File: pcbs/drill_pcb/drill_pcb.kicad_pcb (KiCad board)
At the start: 2 copper layers, 85 parts, among them J301 Screw_Terminal_01x06, J302 motor1, J303 Screw_Terminal_01x03, J304 Screw_Terminal_01x03, J305 Screw_Terminal_01x06, J306 motor2, J307 TOF_senzor, J308 Screw_Terminal_01x03, J309 Screw_Terminal_01x03, J401 Screw_Terminal_01x04, J402 Screw_Terminal_01x06, J403 Screw_Terminal_01x04, SW101 RPi reset, SW401 SW_Push, SW402 SW_Push, SW403 SW_Push, U101 PCA9306, U102 Pico, U201 IFX007T, U202 IFX007T, U203 ACS712xLCTR-20A, U401 HT75xx-1-SOT89

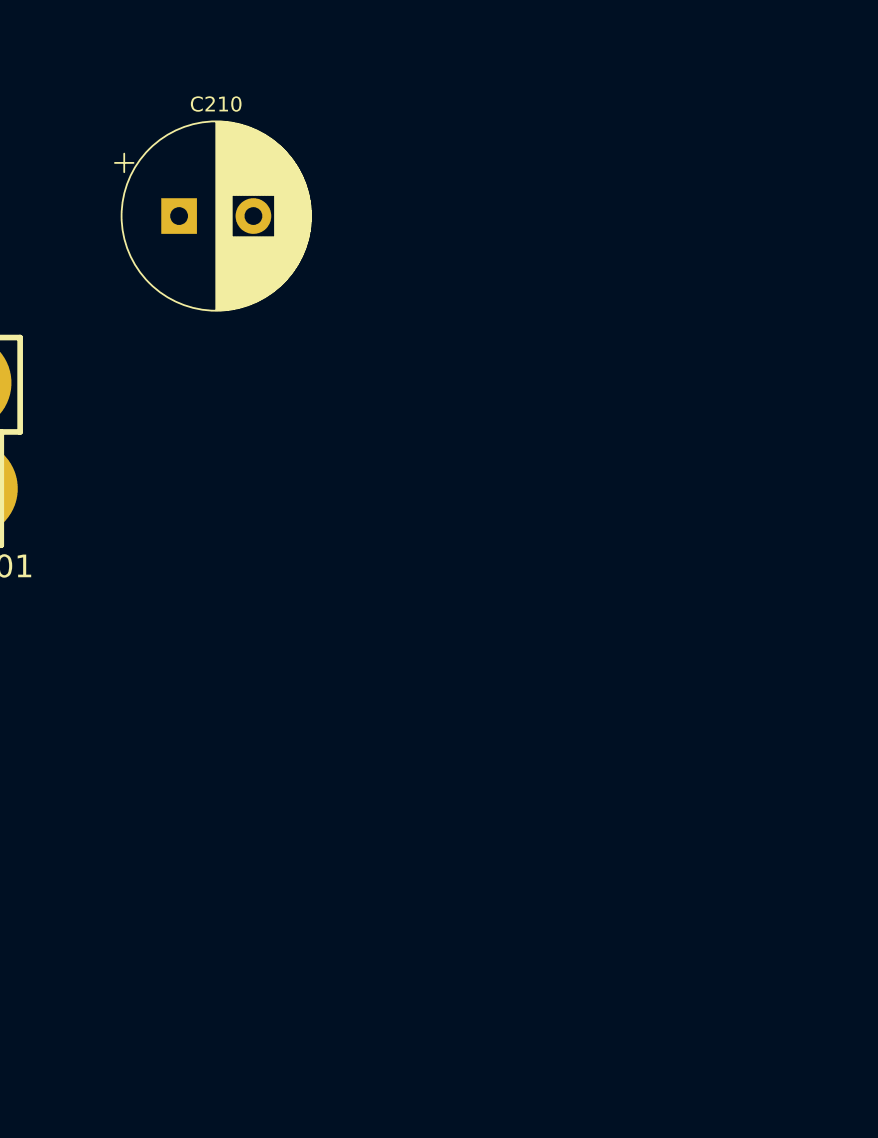
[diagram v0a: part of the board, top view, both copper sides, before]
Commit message: added motor heatsink footprint
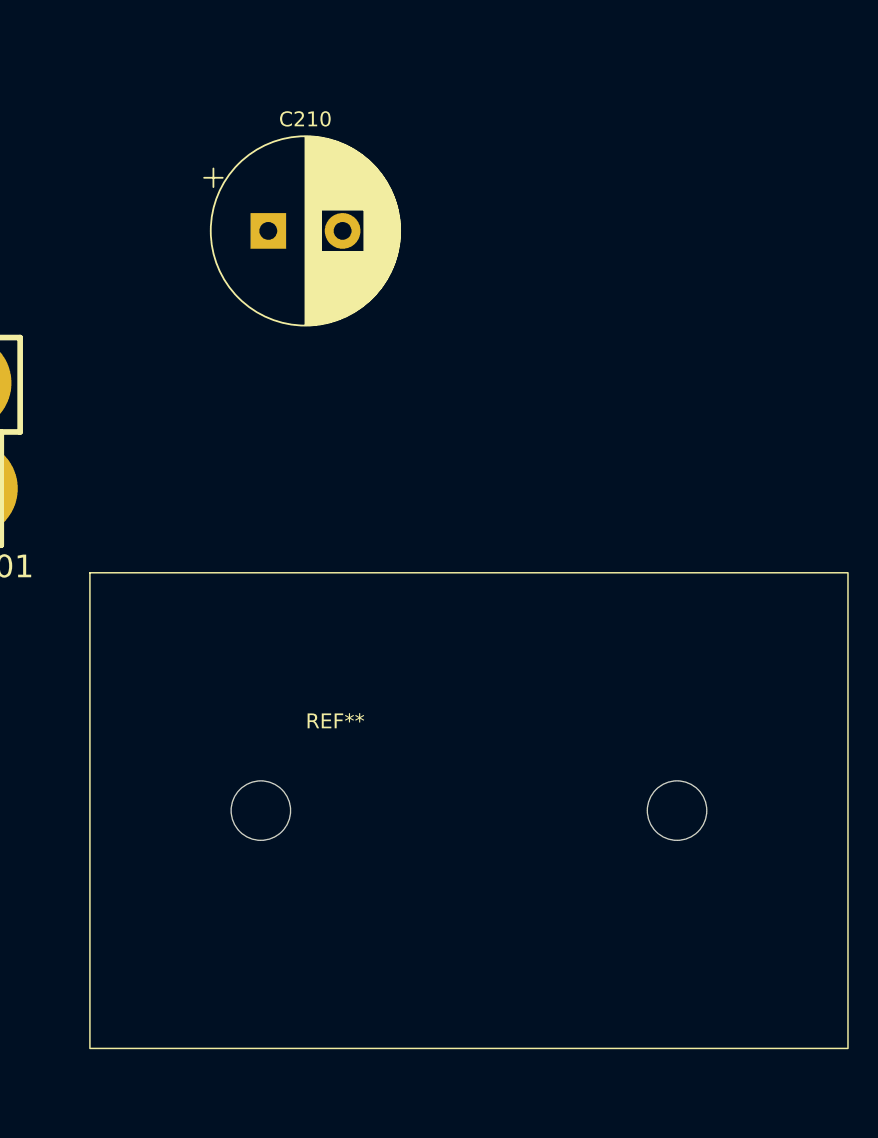
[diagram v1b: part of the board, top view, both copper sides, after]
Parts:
- added REF**: drill_heatsink, heatsink:drill_heatsink, F.Cu at (348.0, 85.0)
- moved C210 6.08 mm to (360.0, 62.0)
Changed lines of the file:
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@@
 		)
 	)
+	(footprint "heatsink:drill_heatsink"
+		(layer "F.Cu")
+		(at 348 85)
+		(property "Reference" "REF**"
+			(at 16.5 10 0)
+			(unlocked yes)
+			(layer "F.SilkS")
+			(effects
+				(font
+					(size 1 1)
+					(thickness 0.1)
+				)
+			)
+		)
+		(property "Value" "drill_heatsink"
+			(at 16.5 11.5 0)
+			(unlocked yes)
+			(layer "F.Fab")
+			(effects
+				(font
+					(size 1 1)
+					(thickness 0.15)
+				)
+			)
+		)
+		(property "Footprint" "heatsink:drill_heatsink"
+			(at 16.5 10.5 0)
+			(unlocked yes)
+			(layer "F.Fab")
+			(hide yes)
+			(effects
+				(font
+					(size 1 1)
+					(thickness 0.15)
+				)
+			)
+		)
+		(property "Datasheet" ""
+			(at 16.5 10.5 0)
+			(unlocked yes)
+			(layer "F.Fab")
+			(hide yes)
+			(effects
+				(font
+					(size 1 1)
+					(thickness 0.15)
+				)
+			)
+		)
+		(property "Description" ""
+			(at 16.5 10.5 0)
+			(unlocked yes)
+			(layer "F.Fab")
+			(hide yes)
+			(effects
+				(font
+					(size 1 1)
+					(thickness 0.15)
+				)
+			)
+		)
+		(attr smd)
+		(fp_rect
+			(start 0 0)
+			(end 51 32)
+			(stroke
+				(width 0.1)
+				(type default)
+			)
+			(fill none)
+			(layer "F.SilkS")
+		)
+		(fp_text user "${REFERENCE}"
+			(at 16.5 13 0)
+			(unlocked yes)
+			(layer "F.Fab")
+			(effects
+				(font
+					(size 1 1)
+					(thickness 0.15)
+				)
+			)
+		)
+		(pad "" np_thru_hole circle
+			(at 11.5 16)
+			(size 4 4)
+			(drill 4)
+			(layers "F&B.Cu" "*.Mask")
+		)
+		(pad "" np_thru_hole circle
+			(at 39.5 16)
+			(size 4 4)
+			(drill 4)
+			(layers "F&B.Cu" "*.Mask")
+		)
+	)
 	(footprint "Capacitor_THT:CP_Radial_D5.0mm_P2.50mm"
 		(layer "F.Cu")
@@
 		(tags "Diode SMC (DO-214AB) Handsoldering")
 		(property "Reference" "D101"
-			(at 0 -4.1 360)
+			(at 0 -4.1 0)
 			(layer "F.SilkS")
 			(effects
@@
 		)
 		(property "Value" "3A"
-			(at 0 4.2 360)
+			(at 0 4.2 0)
 			(layer "F.Fab")
 			(effects
@@
 		)
 		(fp_text user "${REFERENCE}"
-			(at 0 -1.5 360)
+			(at 0 -1.5 0)
 			(layer "F.Fab")
 			(effects
@@
 	(footprint "Capacitor_THT:CP_Radial_D12.5mm_P5.00mm"
 		(layer "F.Cu")
-		(at 354 61)
+		(at 360 62)
 		(descr "CP, Radial series, Radial, pin pitch=5.00mm, , diameter=12.5mm, Electrolytic Capacitor")
 		(tags "CP Radial series Radial pin pitch 5.00mm  diameter 12.5mm Electrolytic Capacitor")
@@
 		(tags "car blade fuse")
 		(property "Reference" "F101"
-			(at 4.65 -3.9 360)
+			(at 4.65 -3.9 0)
 			(layer "F.SilkS")
 			(effects
@@
 		)
 		(property "Value" "5A"
-			(at 4.6 4 360)
+			(at 4.6 4 0)
 			(layer "F.Fab")
 			(effects
@@
 		)
 		(fp_text user "${REFERENCE}"
-			(at 4.75 -1.5 360)
+			(at 4.75 -1.5 0)
 			(layer "F.Fab")
 			(effects

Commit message: Mostly finished PCB v1.0.0 Missing strain gauge control circuit
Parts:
- removed C403, C404, C405: 10n, Capacitor_THT:C_Disc_D4.7mm_W2.5mm_P5.00mm
- removed D101: 3A, Diode_SMD:D_SMC_Handsoldering
- removed D401: 1N4007, Diode_THT:D_DO-41_SOD81_P10.16mm_Horizontal
- removed D402, D403, D404: SFH4550, LED_THT:LED_D5.0mm_IRGrey
- removed J303, J304, J308, J309: Screw_Terminal_01x03, Connector_JST:JST_XH_S3B-XH-A-1_1x03_P2.50mm_Horizontal
- removed J305: Screw_Terminal_01x06, Connector_JST:JST_XH_S6B-XH-A-1_1x06_P2.50mm_Horizontal
- removed JST201: Thermometer, Connector_JST:JST_XH_B3B-XH-A_1x03_P2.50mm_Vertical
- removed R401, R402, R403, R404: 10k, Resistor_THT:R_Axial_DIN0207_L6.3mm_D2.5mm_P10.16mm_Horizontal
- removed SW401, SW402, SW403: SW_Push, Button_Switch_THT:SW_PUSH_6mm
- removed U101: PCA9306, drill_i2c_level_shifter:i2c_levl_shifter
- added D203: SMAJ24A, Diode_SMD:D_SMA, F.Cu at (99.0, 154.0)
- added J201: Thermometer, Connector_JST:JST_XH_B3B-XH-A_1x03_P2.50mm_Vertical, F.Cu at (87.5, 193.0)
- added REF**: MountingHole_3.2mm_M3, MountingHole:MountingHole_3.2mm_M3, F.Cu at (285.0, 105.0)
- added REF**: MountingHole_3.2mm_M3, MountingHole:MountingHole_3.2mm_M3, F.Cu at (55.0, 105.0)
- added REF**: MountingHole_3.2mm_M3, MountingHole:MountingHole_3.2mm_M3, F.Cu at (55.0, 195.0)
- added REF**: MountingHole_3.2mm_M3, MountingHole:MountingHole_3.2mm_M3, F.Cu at (285.0, 195.0)
- added U1: FXMA108, drill_i2c_level_shifter:logic_convertor_8ch, F.Cu at (147.0, 111.0)
- C202, C203, C207, R202, R203, R206, R207, R210, R301, REF**: moved to B.Cu
- J401, J403: footprint TerminalBlock_TE-Connectivity:TerminalBlock_TE_282834-4_1x04_P2.54mm_Horizontal -> Connector_JST:JST_XH_B4B-XH-A_1x04_P2.50mm_Vertical
- J402: footprint TerminalBlock_TE-Connectivity:TerminalBlock_TE_282834-6_1x06_P2.54mm_Horizontal -> Connector_JST:JST_XH_B6B-XH-A_1x06_P2.50mm_Vertical
- moved D201 305.8 mm to (56.0, 133.5), turned to 180 degrees
- moved D202 300.0 mm to (54.5, 113.3), turned to 180 degrees
- moved U203 296.2 mm to (82.1, 180.0)
- moved Dean201 289.1 mm to (74.5, 192.6), turned to -90 degrees
- moved C210 286.6 mm to (86.0, 146.0), turned to 90 degrees
- moved U202 286.0 mm to (71.3, 165.7), turned to -90 degrees
- moved C202 282.8 mm to (61.9, 143.5)
- moved C206 282.2 mm to (55.0, 127.0)
- moved U201 281.2 mm to (82.1, 165.7), turned to -90 degrees
- moved C208 280.9 mm to (53.5, 116.8)
- moved C203 276.9 mm to (67.1, 143.5), turned to 180 degrees
- moved C205 276.3 mm to (69.1, 154.5), turned to 180 degrees
- moved R202 276.2 mm to (62.0, 140.5), turned to 180 degrees
- moved C201 276.1 mm to (87.0, 183.5), turned to 90 degrees
- moved R208 275.8 mm to (55.0, 130.0), turned to 180 degrees
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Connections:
- A201 pad 28: unconnected-(A201-~{RESET}-Pad28) -> /Motor control/RESET
- A201 pad 3: unconnected-(A201-~{RESET}-Pad3) -> /Motor control/RESET
- A301 pad 28: unconnected-(A301-~{RESET}-Pad28) -> /Linear drive control/RESET
- A301 pad 3: unconnected-(A301-~{RESET}-Pad3) -> /Linear drive control/RESET
- A401 pad 12: BTN_RED -> unconnected-(A401-D9-Pad12)
- A401 pad 13: BTN_YEL -> unconnected-(A401-D10-Pad13)
- A401 pad 28: unconnected-(A401-~{RESET}-Pad28) -> /Storage and weighing/RESET
- A401 pad 3: unconnected-(A401-~{RESET}-Pad3) -> /Storage and weighing/RESET
- A401 pad 7: BTN_GRN -> unconnected-(A401-D4-Pad7)
- A402 pad 8: +23,3V -> +24V
- C401 pad 1: +23,3V -> +24V
- F102 pad 2: Net-(D101-A) -> Net-(V101-+Vin)
- U102 pad 10: unconnected-(U102-GPIO7-Pad10) -> Net-(U1-A3)
- U102 pad 11: unconnected-(U102-GPIO8-Pad11)_1 -> Net-(U1-A2)
- U102 pad 12: unconnected-(U102-GPIO9-Pad12)_1 -> Net-(U1-A1)
- U401 pad 2: +23,3V -> +24V
- V101 pad 1: Net-(D101-K) -> Net-(V101-+Vin)
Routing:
- net GND: track 0.00 -> 938.0 mm, vias 0 -> 7
- net +5V: track 0.00 -> 548.3 mm, vias 0 -> 1
- net +24V: track 0.00 -> 287.3 mm
- net /Linear drive control/SDA: track 0.00 -> 196.2 mm, vias 0 -> 2
- net /Linear drive control/SCL: track 0.00 -> 194.0 mm
- net Net-(A201-A3): track 0.00 -> 141.6 mm, vias 0 -> 1
- net Net-(A301-A1): track 0.00 -> 136.6 mm
- net Net-(A301-D11): track 0.00 -> 126.3 mm
- net Net-(A201-A0): track 0.00 -> 115.4 mm, vias 0 -> 2
- net Net-(A301-A0): track 0.00 -> 114.6 mm
- net /Storage and weighing/RESET: track 0.00 -> 113.7 mm
- net Net-(A301-D9): track 0.00 -> 113.7 mm
- net Net-(A201-D7): track 0.00 -> 100.3 mm, vias 0 -> 1
- net Net-(A301-D10): track 0.00 -> 96.9 mm
- net Net-(A301-D5): track 0.00 -> 96.3 mm
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- added copper zone on B.Cu, net Net-(Dean201-Pin_2)
- added copper zone on B.Cu, net Net-(U201-OUT-Pad8)
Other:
- board outline added: 240 x 100 mm
- board text added: "Brno Drilling Space Mission v1.0.0"
- board text added: "ŠLÍMA SMRDÍ"

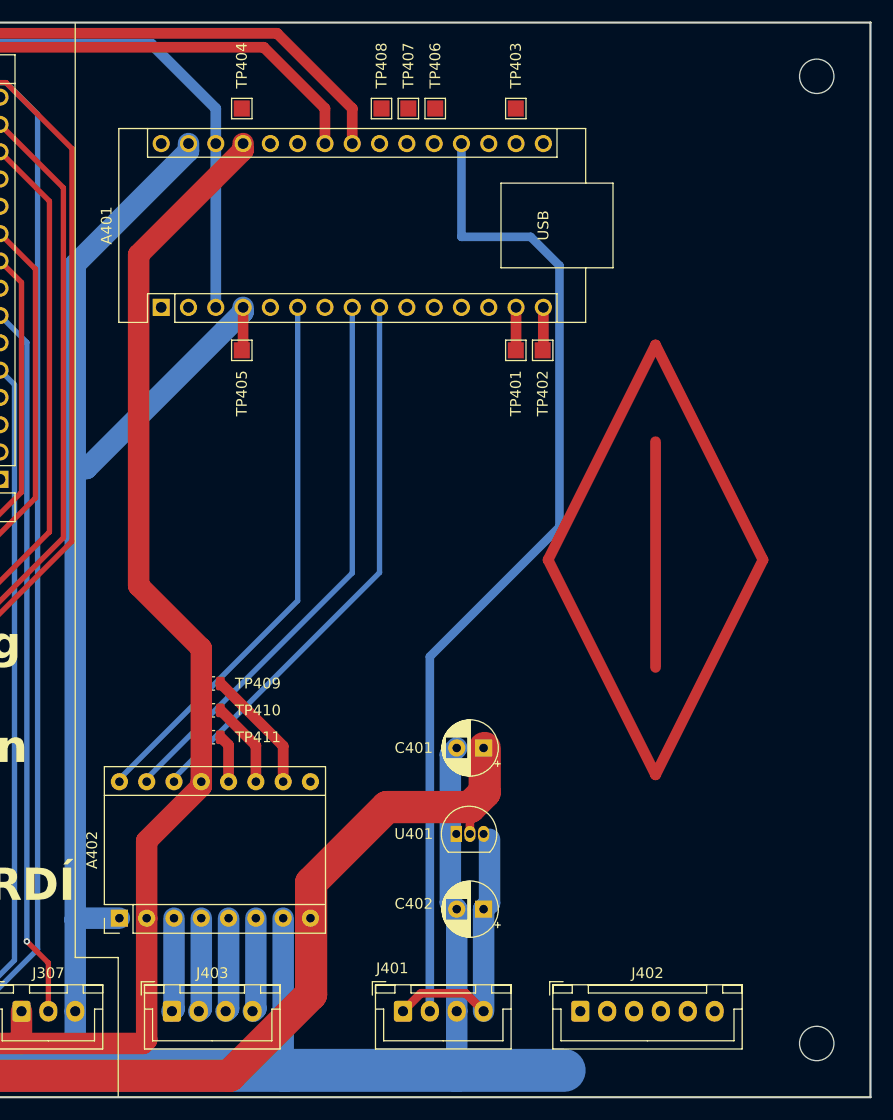
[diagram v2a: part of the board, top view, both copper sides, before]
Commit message: update pouzdra konvertoru
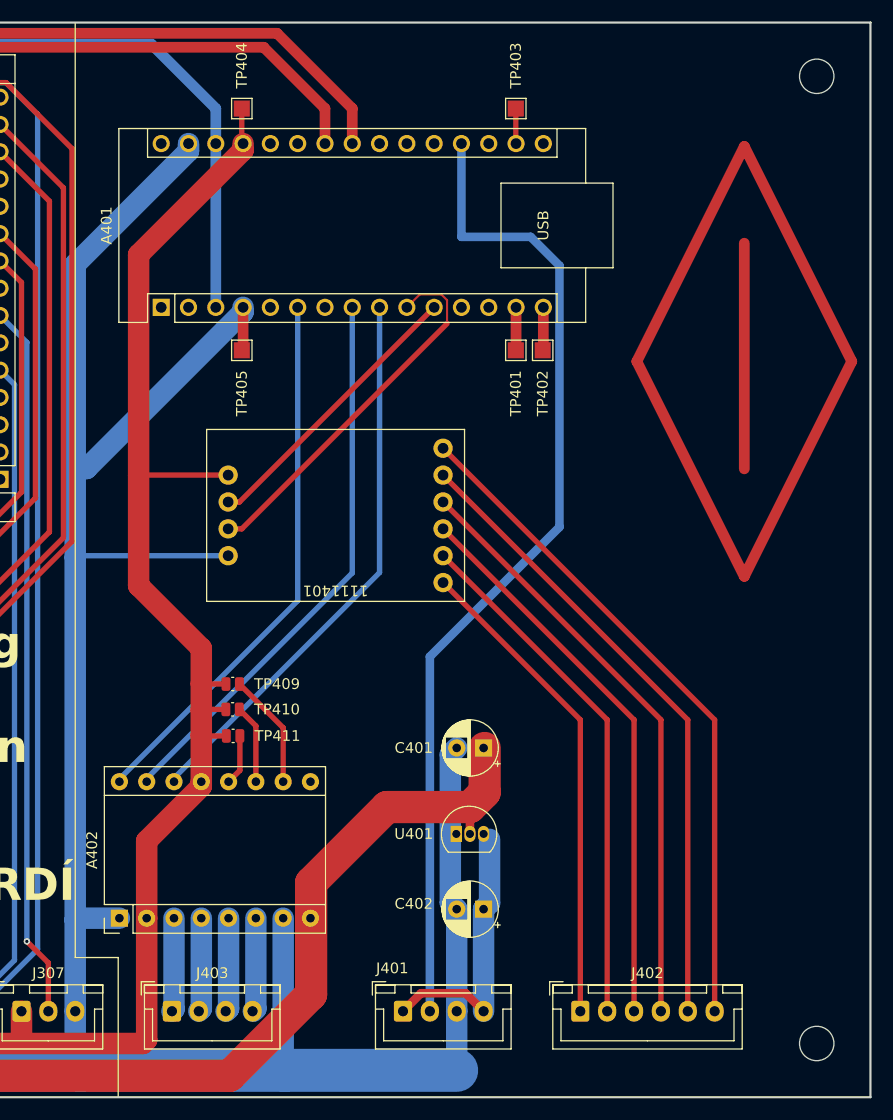
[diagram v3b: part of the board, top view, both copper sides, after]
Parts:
- removed TP406, TP407, TP408: TestPoint, TestPoint:TestPoint_Pad_1.5x1.5mm
- added 1111401: ~, drill_hx711footp:HX711, F.Cu at (240.2, 145.9)
- moved TP411 1.82 mm to (230.7, 166.4)
- moved TP409 1.78 mm to (230.7, 161.6)
- moved TP410 1.77 mm to (230.6, 163.9)
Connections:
- A401 pad 20: Net-(A401-A1) -> unconnected-(A401-A1-Pad20)
- A401 pad 21: Net-(A401-A2) -> unconnected-(A401-A2-Pad21)
- A401 pad 22: Net-(A401-A3) -> unconnected-(A401-A3-Pad22)
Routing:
- net Net-(1111401-B+): track 0.00 -> 62.9 mm
- net Net-(1111401-B-): track 0.00 -> 59.3 mm
- net Net-(1111401-A+): track 0.00 -> 55.8 mm
- net Net-(1111401-A-): track 0.00 -> 52.3 mm
- net Net-(1111401-E-): track 0.00 -> 48.7 mm
- net Net-(1111401-E+): track 0.00 -> 45.2 mm
- net ADC_DT: track 0.00 -> 34.9 mm
- net ADC_SCK: track 0.00 -> 26.7 mm
- net +5V: track 548.3 -> 566.9 mm
- net GND: track 938.0 -> 942.3 mm
- net Net-(A401-3V3): track 0.00 -> 3.27 mm
- net Net-(A402-MS1): track 11.6 -> 10.8 mm
- net Net-(A402-MS2): track 8.00 -> 7.37 mm

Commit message: PCB update
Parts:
- added G***: LOGO, logo:logo, F.Cu at (318.5, 149.0)
- moved U1 78.3 mm to (222.0, 133.5), turned to -90 degrees
- moved SW101 55.2 mm to (168.0, 103.5)
- moved C302 49.8 mm to (231.5, 178.0), turned to 0 degrees
- moved A303 47.5 mm to (226.0, 165.5)
- moved J306 47.4 mm to (220.8, 188.0)
- moved 1111401 45.3 mm to (285.2, 140.9)
- moved A201 45.3 mm to (110.6, 120.2)
- moved A301 45.3 mm to (254.0, 137.5)
- moved A401 45.3 mm to (269.0, 121.5)
- moved A402 45.3 mm to (265.1, 178.3)
- moved C201 45.3 mm to (132.0, 178.5)
- moved C202 45.3 mm to (106.9, 138.5)
- moved C203 45.3 mm to (112.1, 138.5)
- moved C204 45.3 mm to (125.1, 149.5)
- moved C205 45.3 mm to (114.1, 149.5)
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- renumbered REF** to HEATSINK
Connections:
- U1 pad 1: +3.3V -> GND
- U102 pad 1: unconnected-(U102-GPIO0-Pad1)_1 -> GND
- U102 pad 36: +3.3V -> GND
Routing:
- net GND: track 942.3 -> 1014.2 mm
- net +3.3V: track 71.5 -> 0.00 mm
- net /Motor control/RESET: track 92.8 -> 153.5 mm
- net /Linear drive control/RESET: track 88.6 -> 29.1 mm
- net +5V: track 566.9 -> 626.0 mm
- net /Linear drive control/SDA: track 196.2 -> 234.8 mm, vias 2 -> 1
- net /Linear drive control/SCL: track 194.0 -> 231.5 mm
- net +24V: track 287.3 -> 314.4 mm
- net /Storage and weighing/RESET: track 113.7 -> 91.1 mm
- net Net-(A301-D5): track 96.3 -> 111.4 mm
- net Net-(U1-A3): track 21.5 -> 8.95 mm
- net Net-(U1-A2): track 21.5 -> 8.94 mm
- net Net-(U1-A1): track 21.4 -> 8.92 mm
- net Net-(U102-RUN): track 28.5 -> 40.8 mm
- net Net-(A301-D9): track 113.7 -> 122.5 mm
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- added copper zone on B.Cu, net (none)
- added copper zone on F.Cu, net (none)
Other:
- board text added: "RESET"
- board text removed: "ŠLÍMA SMRDÍ"

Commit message: pcb update
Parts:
- 24V IN: renamed from Dean101
- ROTARY ENCODER: renamed from J401
- STRAIN GAUGE: renamed from J402
- TOF SENSOR: renamed from J307
- TOP BOARD: renamed from J301
- renumbered Dean201 to MOTOR, J403 to STEPPER, J302 to STEPPER1, J306 to STEPPER2, J201 to THERMOMETER
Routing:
- net Net-(Dean201-Pin_2): track 23.7 -> 1.03 mm
- net GND: track 1014.2 -> 1031.9 mm
- net Net-(A201-A3): track 141.6 -> 126.2 mm
- net Net-(Dean201-Pin_1): track 10.9 -> 0.69 mm
- net Net-(U201-OUT-Pad8): track 9.53 -> 3.50 mm
- net +5V: track 626.0 -> 623.7 mm
- net Net-(A201-D7): track 100.3 -> 102.2 mm
- net Net-(A201-A1): track 94.5 -> 96.0 mm
- added copper zone on F.Cu, net Net-(Dean201-Pin_1)
- added copper zone on F.Cu, net Net-(Dean201-Pin_2)
- added copper zone on F.Cu, net Net-(U201-OUT-Pad8)
